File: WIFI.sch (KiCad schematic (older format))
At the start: 71 parts, among them P701 WL_DBG, P702 WL_RS232, P703 BT_DBG, U701 U.FL, U702 U.FL, U703 WL1807MOD, U901 ESP-12E, Y701 ANT1/BT, Y702 ANT2/WL

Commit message: Connected WIFI subsheet with ESP8266 and WL1807MOD to SD2 Connected WL1807MOD Bluetoth UART to UART3 Connected A7 Module AT UART to UART6 Connected A7 GPS UART to UART5 Connected A7 HS download to UART7 Connected debug pins to UART1 Connected debug pins to UART2 Added CPU_PWR subsheet to connect power rails to i.MX7 A7 UARTs are routed through level shifter to get from 2.8V to 3.3V All the sheets should be on A3 size now Externel USB is connected to USB_OTG1 Board power sheet is cleared out. Only 4V booster is needed.
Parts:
- removed C901, C902: 10n, Capacitors_SMD:C_0603, symbol C
- removed R601, R602, R901, R902, R903, R905, R906, R907, R908, R909: 100, Resistors_SMD:R_0603, symbol R
- removed R711: 100k, Resistors_SMD:R_0603, symbol R
- removed TP601, TP602, TP701, TP702, TP703, TP704, TP705, TP706, TP707, TP708, TP709, TP710, TP711, TP712, TP713, TP714, TP715, TP716, TP717, TP718, TP719, TP720, TP721, TP722, TP723, TP724, TP725, TP726, TP727, TP728, TP729, TP730, TP731, TP732, TP733: TP, buttons:TP, symbol TP
- added C?: 100n, Capacitors_SMD:C_0603, symbol C
- added P?: ESP_DBG, symbol CONN_01X02
- added R? (x11): 0, symbol R
- added R? (x2): 100k, symbol R
- C701, L701, P701, P702, P703, R703, R705, U701, U702, Y701: manufacture (none) -> DNP
- L703, R707, R709: Manufacturing Information DNP -> (none); manufacture (none) -> DNP
- R904: value R -> 0
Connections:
- net labels added: CCM_CLKO2_32k, NVCC_1V8, NVCC_3V3, NVCC_SD2, SD2_BUS0, SD2_BUS1, SD2_BUS2, SD2_BUS3, SD2_BUS4, SD2_BUS5, SD2_BUS6, SD2_BUS7, SD2_BUS8, SD2_BUS[0..8], SD2_CLK, SD2_CMD, SD2_D0, SD2_D1, SD2_D2, SD2_D3, SD2_WP, SD2_~CD, SD2_~RST
- net labels removed: +1V8, +3V3, CH_PD, ESP_UART0, ESP_UART1, ESP_UART2, ESP_UART3, ESP_UART[0..3], EXT_32K, GPIO0, GPIO12, GPIO13, VCC, WL0, WL1, WL2, WL3, WL4, WL5, WL6, WLAN_EN, WL[0..6], ~INT, ~LINK_UP, ~RESET
- wire segments 122 -> 117
- no-connect marks 9 -> 17
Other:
- note added: "ESP8266 WiFi connectivity option using esp8089 kernel driver"
- note added: "For ESP8266 use 3V3 to power SD2 peripheral.\nFor WL1807MOD use 1V8 to power SD2 peripheral."
- note added: "Peripheral power selection"
- note removed: "0 ->\n1 ->\n2 ->\n3 ->\n"
- note removed: "ESP8266 WiFi connectivity option"
- note removed: "Reserved pins NC as \nmetioned in datasheet"
- note removed: "TX\nRX\nCTS\nRTS"
- note removed: "for debug only"
- moved on the sheet: C701, C702, C703, C704, C705, L701, L702, L703, L704, P701, P702, P703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

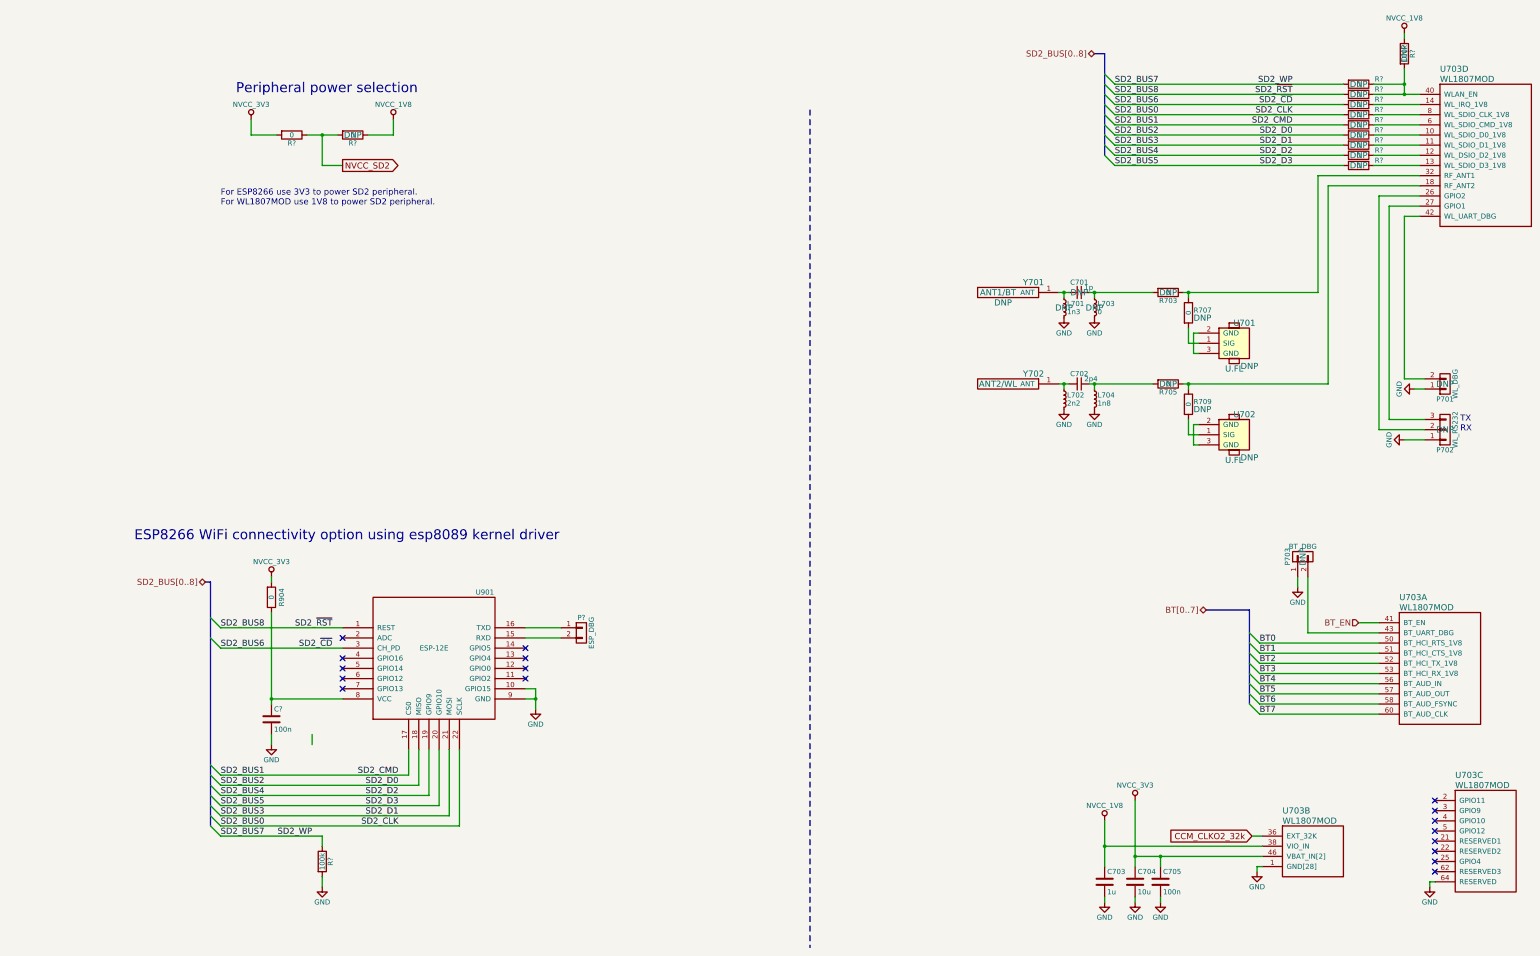
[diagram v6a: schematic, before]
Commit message: Prepare for two battery types NiMH battery for using the original battery pack LiPo battery for using long lasting modern battery
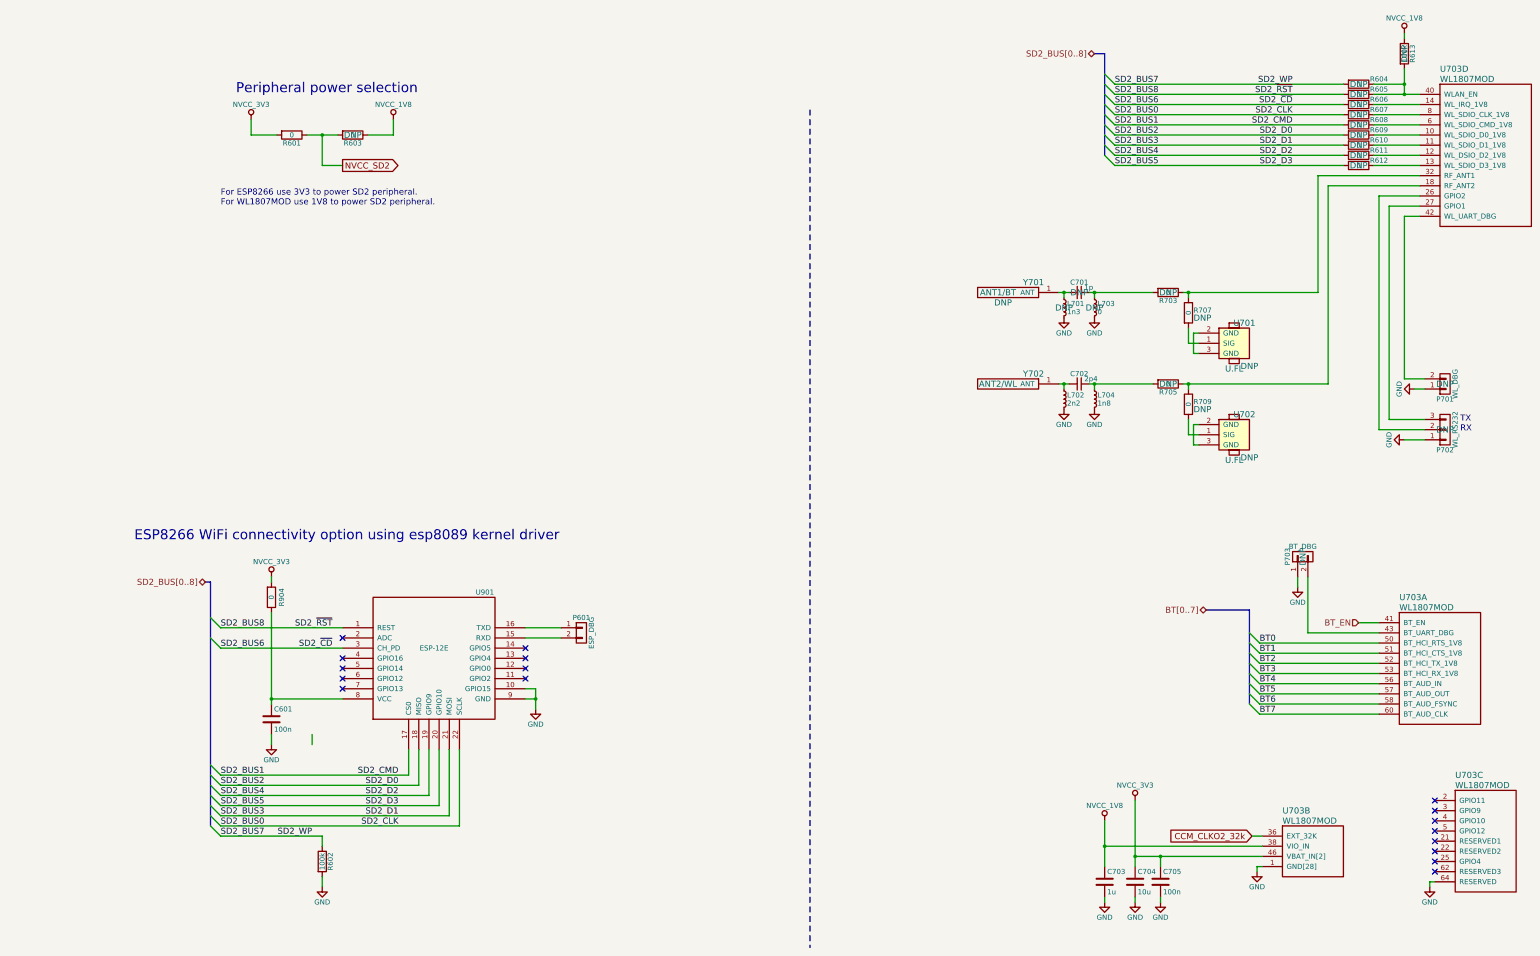
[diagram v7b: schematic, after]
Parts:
- gave numbers to parts that had none: 15
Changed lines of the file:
@@
 EESchema Schematic File Version 2
-LIBS:3210retro-rescue
-LIBS:power
-LIBS:device
-LIBS:transistors
-LIBS:conn
-LIBS:linear
-LIBS:regul
-LIBS:74xx
-LIBS:cmos4000
-LIBS:adc-dac
-LIBS:memory
-LIBS:xilinx
-LIBS:microcontrollers
-LIBS:dsp
-LIBS:microchip
-LIBS:analog_switches
-LIBS:motorola
-LIBS:texas
-LIBS:intel
-LIBS:audio
-LIBS:interface
-LIBS:digital-audio
-LIBS:philips
-LIBS:display
-LIBS:cypress
-LIBS:siliconi
-LIBS:opto
-LIBS:atmel
-LIBS:contrib
-LIBS:valves
 LIBS:a7
 LIBS:ft232rl
@@
 LIBS:sn74avc2t244
 LIBS:lsm9ds1
+LIBS:WM8960CGEFL
+LIBS:tps61021a
+LIBS:bq24400
+LIBS:power
+LIBS:device
+LIBS:transistors
+LIBS:conn
+LIBS:linear
+LIBS:regul
+LIBS:74xx
+LIBS:cmos4000
+LIBS:adc-dac
+LIBS:memory
+LIBS:xilinx
+LIBS:microcontrollers
+LIBS:dsp
+LIBS:microchip
+LIBS:analog_switches
+LIBS:motorola
+LIBS:texas
+LIBS:intel
+LIBS:audio
+LIBS:interface
+LIBS:digital-audio
+LIBS:philips
+LIBS:display
+LIBS:cypress
+LIBS:siliconi
+LIBS:opto
+LIBS:atmel
+LIBS:contrib
+LIBS:valves
 LIBS:3210retro-cache
 EELAYER 25 0
@@
 	3100 7350 3800 7350
 $Comp
-L GND #PWR060
+L GND #PWR606
 U 1 1 584B4036
 P 5700 7450
-F 0 "#PWR060" H 5700 7200 50  0001 C CNN
+F 0 "#PWR606" H 5700 7200 50  0001 C CNN
 F 1 "GND" H 5700 7300 50  0000 C CNN
 F 2 "" H 5700 7450 50  0000 C CNN
@@
 NoConn ~ 14550 8350
 $Comp
-L GND #PWR062
+L GND #PWR621
 U 1 1 585926BC
 P 14500 9200
-F 0 "#PWR062" H 14500 8950 50  0001 C CNN
+F 0 "#PWR621" H 14500 8950 50  0001 C CNN
 F 1 "GND" H 14500 9050 50  0000 C CNN
 F 2 "" H 14500 9200 50  0000 C CNN
@@
 	12750 8700 12850 8700
 $Comp
-L GND #PWR063
+L GND #PWR616
 U 1 1 5859516A
 P 12800 9050
-F 0 "#PWR063" H 12800 8800 50  0001 C CNN
+F 0 "#PWR616" H 12800 8800 50  0001 C CNN
 F 1 "GND" H 12800 8900 50  0000 C CNN
 F 2 "" H 12800 9050 50  0000 C CNN
@@
 Connection ~ 11300 8800
 $Comp
-L GND #PWR064
+L GND #PWR612
 U 1 1 58595866
 P 11300 9350
-F 0 "#PWR064" H 11300 9100 50  0001 C CNN
+F 0 "#PWR612" H 11300 9100 50  0001 C CNN
 F 1 "GND" H 11300 9200 50  0000 C CNN
 F 2 "" H 11300 9350 50  0000 C CNN
@@
 $EndComp
 $Comp
-L GND #PWR065
+L GND #PWR614
 U 1 1 585958AA
 P 11600 9350
-F 0 "#PWR065" H 11600 9100 50  0001 C CNN
+F 0 "#PWR614" H 11600 9100 50  0001 C CNN
 F 1 "GND" H 11600 9200 50  0000 C CNN
 F 2 "" H 11600 9350 50  0000 C CNN
@@
 $EndComp
 $Comp
-L GND #PWR066
+L GND #PWR615
 U 1 1 585958EE
 P 11850 9350
-F 0 "#PWR066" H 11850 9100 50  0001 C CNN
+F 0 "#PWR615" H 11850 9100 50  0001 C CNN
 F 1 "GND" H 11850 9200 50  0000 C CNN
 F 2 "" H 11850 9350 50  0000 C CNN
@@
 $EndComp
 $Comp
-L GND #PWR069
+L GND #PWR617
 U 1 1 58594C19
 P 13200 6250
-F 0 "#PWR069" H 13200 6000 50  0001 C CNN
+F 0 "#PWR617" H 13200 6000 50  0001 C CNN
 F 1 "GND" H 13200 6100 50  0000 C CNN
 F 2 "" H 13200 6250 50  0000 C CNN
@@
 $EndComp
 $Comp
-L GND #PWR070
+L GND #PWR620
 U 1 1 58595855
 P 14350 4300
-F 0 "#PWR070" H 14350 4050 50  0001 C CNN
+F 0 "#PWR620" H 14350 4050 50  0001 C CNN
 F 1 "GND" H 14350 4150 50  0000 C CNN
 F 2 "" H 14350 4300 50  0000 C CNN
@@
 $EndComp
 $Comp
-L GND #PWR071
+L GND #PWR608
 U 1 1 58597FAF
 P 10900 4500
-F 0 "#PWR071" H 10900 4250 50  0001 C CNN
+F 0 "#PWR608" H 10900 4250 50  0001 C CNN
 F 1 "GND" H 10900 4350 50  0000 C CNN
 F 2 "" H 10900 4500 50  0000 C CNN
@@
 Connection ~ 10900 4250
 $Comp
-L GND #PWR072
+L GND #PWR607
 U 1 1 585982F6
 P 10900 3600
-F 0 "#PWR072" H 10900 3350 50  0001 C CNN
+F 0 "#PWR607" H 10900 3350 50  0001 C CNN
 F 1 "GND" H 10900 3450 50  0000 C CNN
 F 2 "" H 10900 3600 50  0000 C CNN
@@
 $EndComp
 $Comp
-L GND #PWR073
+L GND #PWR610
 U 1 1 585984EA
 P 11200 4500
-F 0 "#PWR073" H 11200 4250 50  0001 C CNN
+F 0 "#PWR610" H 11200 4250 50  0001 C CNN
 F 1 "GND" H 11200 4350 50  0000 C CNN
 F 2 "" H 11200 4500 50  0000 C CNN
@@
 $EndComp
 $Comp
-L GND #PWR074
+L GND #PWR609
 U 1 1 58598B81
 P 11200 3600
-F 0 "#PWR074" H 11200 3350 50  0001 C CNN
+F 0 "#PWR609" H 11200 3350 50  0001 C CNN
 F 1 "GND" H 11200 3450 50  0000 C CNN
 F 2 "" H 11200 3600 50  0000 C CNN
@@
 	12725 6475 12300 6475
 $Comp
-L NVCC_3V3 #PWR?
+L NVCC_3V3 #PWR602
 U 1 1 59432FA3
 P 3100 6150
-F 0 "#PWR?" H 3100 6000 50  0001 C CNN
+F 0 "#PWR602" H 3100 6000 50  0001 C CNN
 F 1 "NVCC_3V3" H 3100 6300 50  0000 C CNN
 F 2 "" H 3100 6150 50  0001 C CNN
@@
 NoConn ~ 3800 6950
 $Comp
-L CONN_01X02 P?
+L CONN_01X02 P601
 U 1 1 5943396E
 P 6150 6700
-F 0 "P?" H 6150 6850 50  0000 C CNN
+F 0 "P601" H 6150 6850 50  0000 C CNN
 F 1 "ESP_DBG" V 6250 6700 50  0000 C CNN
 F 2 "" H 6150 6700 50  0000 C CNN
@@
 NoConn ~ 5600 7150
 $Comp
-L C C?
+L C C601
 U 1 1 594340D2
 P 3100 7550
-F 0 "C?" H 3125 7650 50  0000 L CNN
+F 0 "C601" H 3125 7650 50  0000 L CNN
 F 1 "100n" H 3125 7450 50  0000 L CNN
 F 2 "Capacitors_SMD:C_0603" H 3138 7400 50  0001 C CNN
@@
 	3100 6500 3100 7400
 $Comp
-L GND #PWR?
+L GND #PWR603
 U 1 1 5943453A
 P 3100 7800
-F 0 "#PWR?" H 3100 7550 50  0001 C CNN
+F 0 "#PWR603" H 3100 7550 50  0001 C CNN
 F 1 "GND" H 3100 7650 50  0000 C CNN
 F 2 "" H 3100 7800 50  0000 C CNN
@@
 	2500 8500 2600 8600
 $Comp
-L R R?
+L R R601
 U 1 1 59441477
 P 3300 1800
-F 0 "R?" V 3380 1800 50  0000 C CNN
+F 0 "R601" V 3380 1800 50  0000 C CNN
 F 1 "0" V 3300 1800 50  0000 C CNN
 F 2 "" V 3230 1800 50  0000 C CNN
@@
 $EndComp
 $Comp
-L NVCC_3V3 #PWR?
+L NVCC_3V3 #PWR601
 U 1 1 5944147E
 P 2900 1650
-F 0 "#PWR?" H 2900 1500 50  0001 C CNN
+F 0 "#PWR601" H 2900 1500 50  0001 C CNN
 F 1 "NVCC_3V3" H 2900 1800 50  0000 C CNN
 F 2 "" H 2900 1650 50  0001 C CNN
@@
 $EndComp
 $Comp
-L R R?
+L R R603
 U 1 1 59441487
 P 3900 1800
-F 0 "R?" V 3980 1800 50  0000 C CNN
+F 0 "R603" V 3980 1800 50  0000 C CNN
 F 1 "0" V 3900 1800 50  0000 C CNN
 F 2 "" V 3830 1800 50  0000 C CNN
@@
 	14250 1150 14250 1400
 $Comp
-L R R?
+L R R613
 U 1 1 59443EB4
 P 14250 1000
-F 0 "R?" V 14330 1000 50  0000 C CNN
+F 0 "R613" V 14330 1000 50  0000 C CNN
 F 1 "100k" V 14250 1000 50  0000 C CNN
 F 2 "" V 14180 1000 50  0000 C CNN
@@
 	14250 850  14250 800
 $Comp
-L NVCC_1V8 #PWR?
+L NVCC_1V8 #PWR618
 U 1 1 59445073
 P 14250 800
-F 0 "#PWR?" H 14250 650 50  0001 C CNN
+F 0 "#PWR618" H 14250 650 50  0001 C CNN
 F 1 "NVCC_1V8" H 14250 950 50  0000 C CNN
 F 2 "" H 14250 800 50  0001 C CNN
@@
 $EndComp
 $Comp
-L NVCC_1V8 #PWR?
+L NVCC_1V8 #PWR605
 U 1 1 59445109
 P 4300 1650
-F 0 "#PWR?" H 4300 1500 50  0001 C CNN
+F 0 "#PWR605" H 4300 1500 50  0001 C CNN
 F 1 "NVCC_1V8" H 4300 1800 50  0000 C CNN
 F 2 "" H 4300 1650 50  0001 C CNN
@@
 $EndComp
 $Comp
-L NVCC_1V8 #PWR?
+L NVCC_1V8 #PWR611
 U 1 1 5944519B
 P 11300 8550
-F 0 "#PWR?" H 11300 8400 50  0001 C CNN
+F 0 "#PWR611" H 11300 8400 50  0001 C CNN
 F 1 "NVCC_1V8" H 11300 8700 50  0000 C CNN
 F 2 "" H 11300 8550 50  0001 C CNN
@@
 $EndComp
 $Comp
-L NVCC_3V3 #PWR?
+L NVCC_3V3 #PWR613
 U 1 1 59445234
 P 11600 8350
-F 0 "#PWR?" H 11600 8200 50  0001 C CNN
+F 0 "#PWR613" H 11600 8200 50  0001 C CNN
 F 1 "NVCC_3V3" H 11600 8500 50  0000 C CNN
 F 2 "" H 11600 8350 50  0001 C CNN
@@
 	3600 8700 3600 8800
 $Comp
-L R R?
+L R R602
 U 1 1 5944C38D
 P 3600 8950
-F 0 "R?" V 3680 8950 50  0000 C CNN
+F 0 "R602" V 3680 8950 50  0000 C CNN
 F 1 "100k" V 3600 8950 50  0000 C CNN
 F 2 "" V 3530 8950 50  0000 C CNN
@@
 $EndComp
 $Comp
-L GND #PWR?
+L GND #PWR604
 U 1 1 5944C573
 P 3600 9200
-F 0 "#PWR?" H 3600 8950 50  0001 C CNN
+F 0 "#PWR604" H 3600 8950 50  0001 C CNN
 F 1 "GND" H 3600 9050 50  0000 C CNN
 F 2 "" H 3600 9200 50  0000 C CNN
@@
 	3600 9100 3600 9200
 $Comp
-L GND #PWR?
+L GND #PWR619
 U 1 1 5944DF54
 P 14250 4800
-F 0 "#PWR?" H 14250 4550 50  0001 C CNN
+F 0 "#PWR619" H 14250 4550 50  0001 C CNN
 F 1 "GND" H 14250 4650 50  0000 C CNN
 F 2 "" H 14250 4800 50  0000 C CNN
@@
 	8400 1550 8400 9800
 $Comp
-L R R?
+L R R605
 U 1 1 5945AC4A
 P 13800 1400
-F 0 "R?" V 13750 1600 50  0000 C CNN
+F 0 "R605" V 13750 1600 50  0000 C CNN
 F 1 "0" V 13800 1400 50  0000 C CNN
 F 2 "" V 13730 1400 50  0000 C CNN
@@
 	13950 2100 14400 2100
 $Comp
-L R R?
+L R R604
 U 1 1 5945BED7
 P 13800 1300
-F 0 "R?" V 13750 1500 50  0000 C CNN
+F 0 "R604" V 13750 1500 50  0000 C CNN
 F 1 "0" V 13800 1300 50  0000 C CNN
 F 2 "" V 13730 1300 50  0000 C CNN
@@
 $EndComp
 $Comp
-L R R?
+L R R606
 U 1 1 5945BF51
 P 13800 1500
-F 0 "R?" V 13750 1700 50  0000 C CNN
+F 0 "R606" V 13750 1700 50  0000 C CNN
 F 1 "0" V 13800 1500 50  0000 C CNN
 F 2 "" V 13730 1500 50  0000 C CNN
@@
 $EndComp
 $Comp
-L R R?
+L R R607
 U 1 1 5945BFD0
 P 13800 1600
-F 0 "R?" V 13750 1800 50  0000 C CNN
+F 0 "R607" V 13750 1800 50  0000 C CNN
 F 1 "0" V 13800 1600 50  0000 C CNN
 F 2 "" V 13730 1600 50  0000 C CNN
@@
 $EndComp
 $Comp
-L R R?
+L R R609
 U 1 1 5945C0EE
 P 13800 1800
-F 0 "R?" V 13750 2000 50  0000 C CNN
+F 0 "R609" V 13750 2000 50  0000 C CNN
 F 1 "0" V 13800 1800 50  0000 C CNN
 F 2 "" V 13730 1800 50  0000 C CNN
@@
 $EndComp
 $Comp
-L R R?
+L R R608
 U 1 1 5945C0F5
 P 13800 1700
-F 0 "R?" V 13750 1900 50  0000 C CNN
+F 0 "R608" V 13750 1900 50  0000 C CNN
 F 1 "0" V 13800 1700 50  0000 C CNN
 F 2 "" V 13730 1700 50  0000 C CNN
@@
 $EndComp
 $Comp
-L R R?
+L R R610
 U 1 1 5945C0FC
 P 13800 1900
-F 0 "R?" V 13750 2100 50  0000 C CNN
+F 0 "R610" V 13750 2100 50  0000 C CNN
 F 1 "0" V 13800 1900 50  0000 C CNN
 F 2 "" V 13730 1900 50  0000 C CNN
@@
 $EndComp
 $Comp
-L R R?
+L R R611
 U 1 1 5945C103
 P 13800 2000
-F 0 "R?" V 13750 2200 50  0000 C CNN
+F 0 "R611" V 13750 2200 50  0000 C CNN
 F 1 "0" V 13800 2000 50  0000 C CNN
 F 2 "" V 13730 2000 50  0000 C CNN
@@
 $EndComp
 $Comp
-L R R?
+L R R612
 U 1 1 5945C15A
 P 13800 2100
-F 0 "R?" V 13750 2300 50  0000 C CNN
+F 0 "R612" V 13750 2300 50  0000 C CNN
 F 1 "0" V 13800 2100 50  0000 C CNN
 F 2 "" V 13730 2100 50  0000 C CNN

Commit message: Changed several voltage rail connections Removed non existing rails Added circuit for NiMH charging
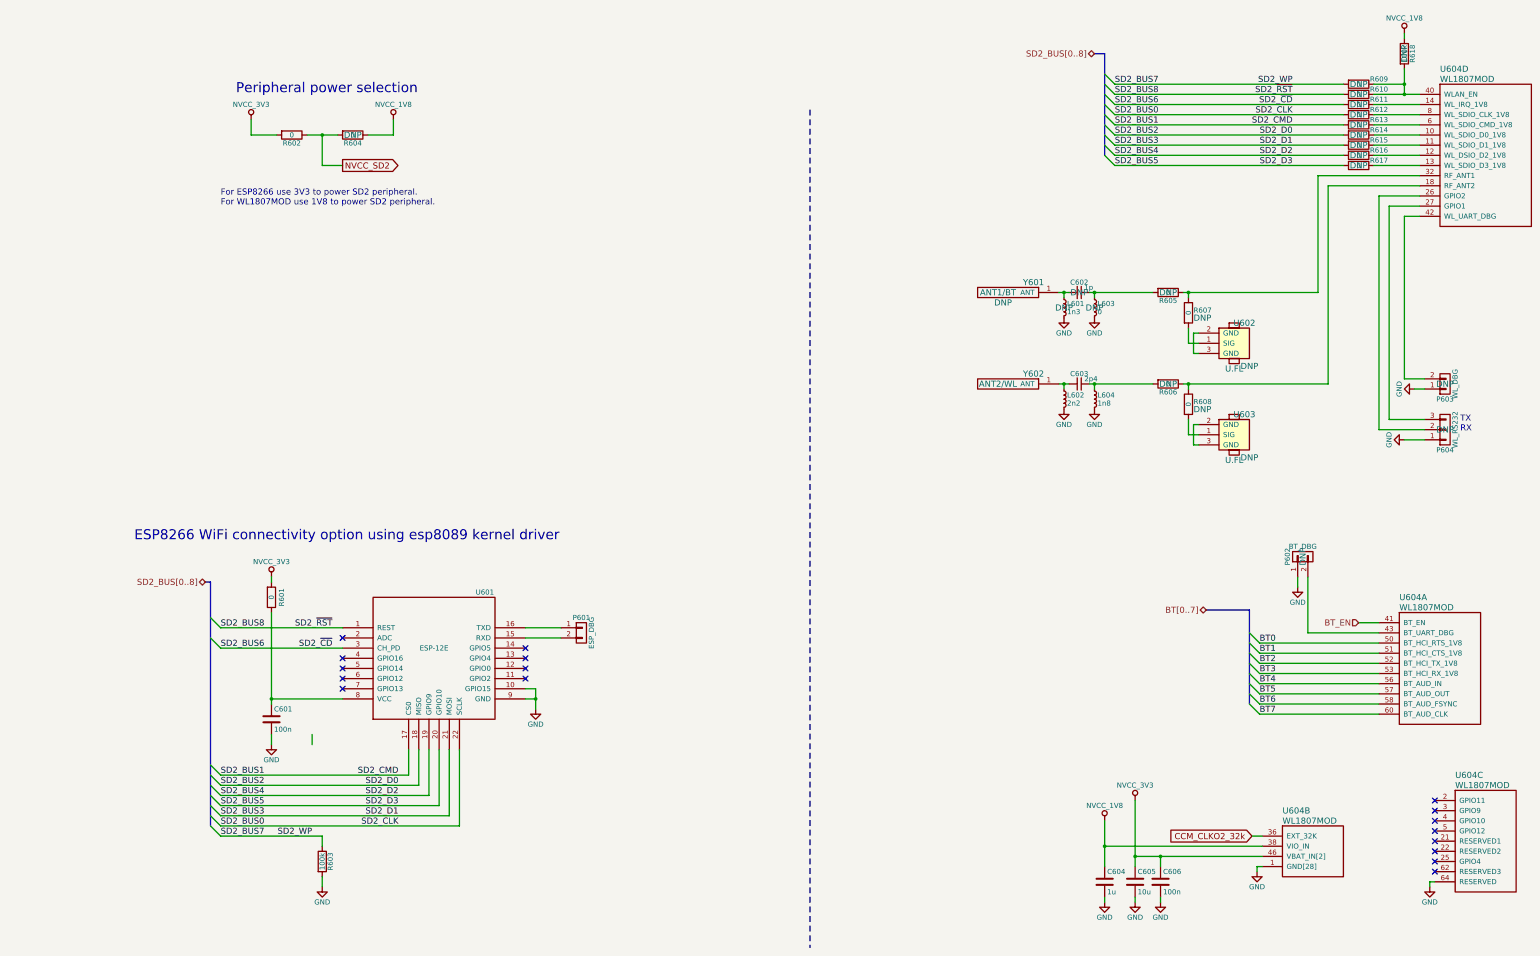
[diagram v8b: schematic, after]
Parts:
- renumbered C701 to C602, C702 to C603, C703 to C604, C704 to C605, C705 to C606, L701 to L601, L702 to L602, L703 to L603, L704 to L604, P703 to P602, P701 to P603, P702 to P604, R904 to R601, R601 to R602, R602 to R603, R603 to R604, R703 to R605, R705 to R606, R707 to R607, R709 to R608, R604 to R609, R605 to R610, R606 to R611, R607 to R612, R608 to R613, R609 to R614, R610 to R615, R611 to R616, R612 to R617, R613 to R618, U901 to U601, U701 to U602, U702 to U603, U703 to U604, Y701 to Y601, Y702 to Y602
